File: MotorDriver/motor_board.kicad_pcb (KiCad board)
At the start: 2 copper layers, 60 x 71 mm, 67 parts, among them J1 Conn_01x04_Socket, J10 Conn_01x04_Socket, J4 Screw_Terminal_01x02, J5 Screw_Terminal_01x04, J6 Screw_Terminal_01x04, J7 Conn_01x16_Socket, J8 Conn_01x16_Socket, J9 Conn_01x16_Socket, Q1 AON6411, U1 PCA9685PW, U2 TB6612FNG, U3 TB6612FNG

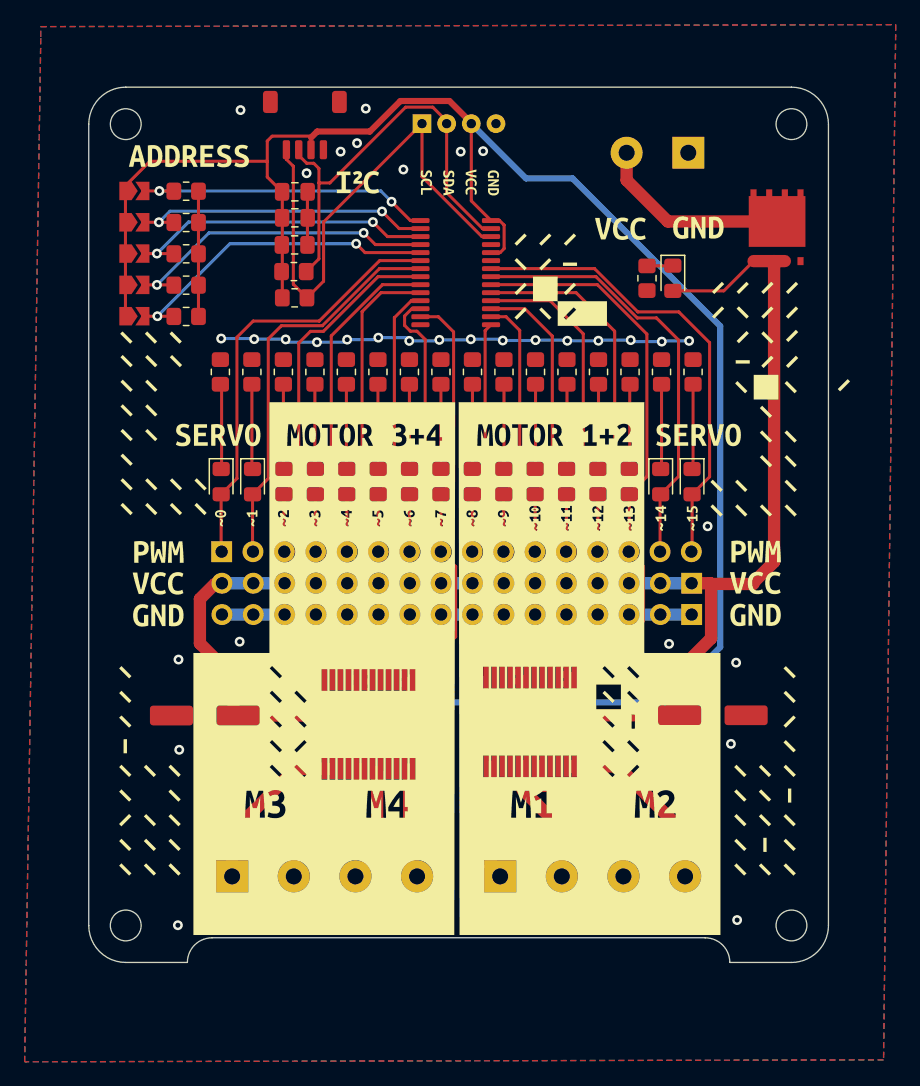
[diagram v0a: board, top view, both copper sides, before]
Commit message: added IMU
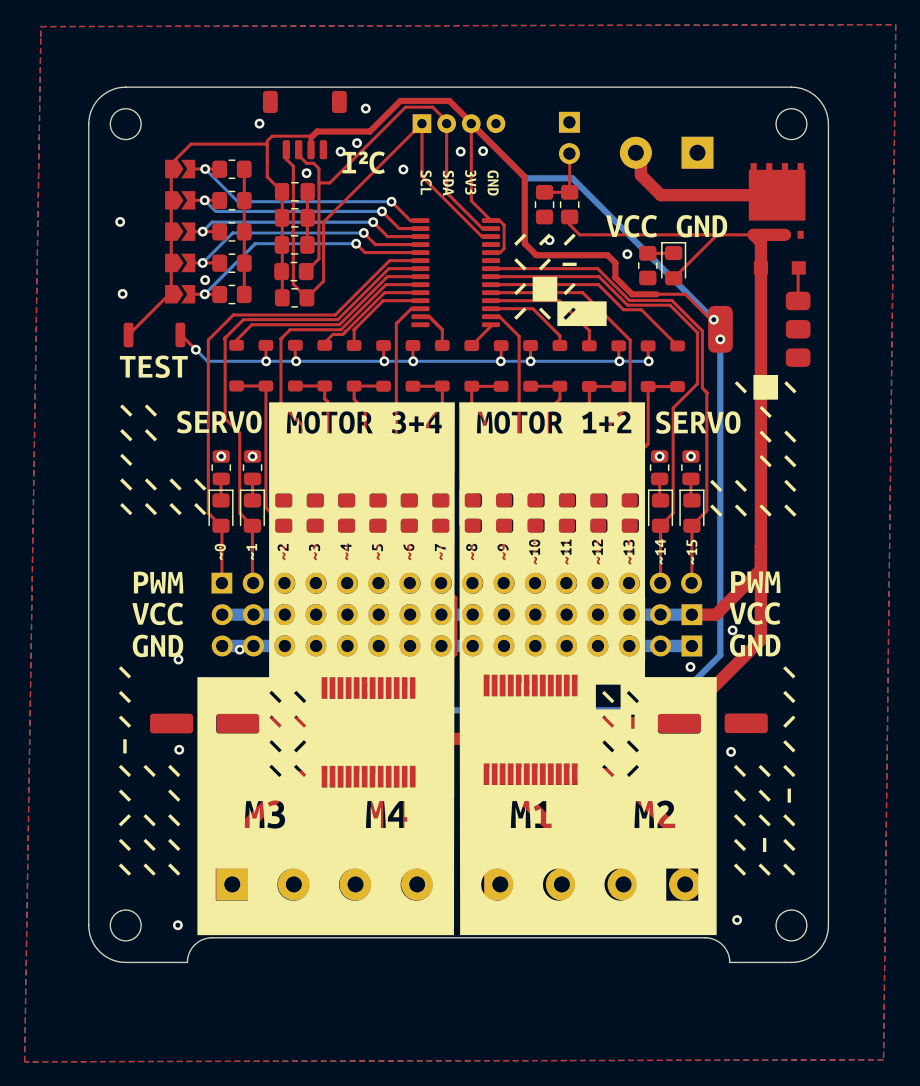
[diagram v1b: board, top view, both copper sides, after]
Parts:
- removed R25: 280, Resistor_SMD:R_0805_2012Metric_Pad1.20x1.40mm_HandSolder
- added CR1: MBR120VLSFT1G, MBR120:SDO_SOD-123FL_ONS, F.Cu at (156.1, 66.7)
- added D1: 1N4148W, Diode_SMD:D_SOD-123, F.Cu at (112.0, 74.6)
- added D19: 1N4148W, Diode_SMD:D_SOD-123, F.Cu at (114.4, 74.6)
- added D20: 1N4148W, Diode_SMD:D_SOD-123, F.Cu at (116.8, 74.6)
- added D21: 1N4148W, Diode_SMD:D_SOD-123, F.Cu at (119.1, 74.6)
- added D22: 1N4148W, Diode_SMD:D_SOD-123, F.Cu at (121.5, 74.6)
- added D23: 1N4148W, Diode_SMD:D_SOD-123, F.Cu at (123.9, 74.6)
- added D24: 1N4148W, Diode_SMD:D_SOD-123, F.Cu at (128.7, 74.6)
- added D25: 1N4148W, Diode_SMD:D_SOD-123, F.Cu at (126.3, 74.6)
- added D26: 1N4148W, Diode_SMD:D_SOD-123, F.Cu at (131.1, 74.6)
- added D27: 1N4148W, Diode_SMD:D_SOD-123, F.Cu at (133.5, 74.6)
- added D28: 1N4148W, Diode_SMD:D_SOD-123, F.Cu at (138.2, 74.6)
- added D29: 1N4148W, Diode_SMD:D_SOD-123, F.Cu at (135.8, 74.6)
- added D30: 1N4148W, Diode_SMD:D_SOD-123, F.Cu at (140.6, 74.6)
- added D31: 1N4148W, Diode_SMD:D_SOD-123, F.Cu at (143.0, 74.6)
- added D32: 1N4148W, Diode_SMD:D_SOD-123, F.Cu at (147.8, 74.6)
- added D33: 1N4148W, Diode_SMD:D_SOD-123, F.Cu at (145.4, 74.6)
- added J3: Conn_01x02_Socket, Connector_PinHeader_2.54mm:PinHeader_1x02_P2.54mm_Vertical, F.Cu at (139.0, 54.9)
- added R26: 1k1, Resistor_SMD:R_0805_2012Metric_Pad1.20x1.40mm_HandSolder, F.Cu at (137.0, 61.5)
- added R27: 3k9, Resistor_SMD:R_0805_2012Metric_Pad1.20x1.40mm_HandSolder, F.Cu at (139.0, 61.5)
- added R8: 270, Resistor_SMD:R_0805_2012Metric, F.Cu at (143.8, 82.9)
- added SW9: SW_Push, Button_Switch_SMD:SW_Push_SPST_NO_Alps_SKRK, F.Cu at (105.3, 72.1)
- added U4: AMS1117, Package_TO_SOT_SMD:SOT-223-3_TabPin2, F.Cu at (154.4, 71.6)
- R10, R11, R12, R13, R14, R15, R16, R17, R18, R19, R20, R21, R22, R23, R24: value 280 -> 270; footprint Resistor_SMD:R_0805_2012Metric_Pad1.20x1.40mm_HandSolder -> Resistor_SMD:R_0805_2012Metric
- moved R23 39.0 mm to (148.8, 82.9)
- moved R24 8.22 mm to (146.3, 82.9)
- moved R10 8.21 mm to (141.2, 82.9)
- moved R11 8.21 mm to (138.7, 82.9)
- moved R12 8.20 mm to (136.1, 82.9)
- moved R13 8.20 mm to (133.6, 82.9)
- moved R14 8.19 mm to (131.1, 82.9)
- moved R15 8.19 mm to (128.5, 82.9)
- moved R16 8.18 mm to (126.0, 82.9)
- moved R17 8.18 mm to (123.4, 82.9)
- moved R18 8.17 mm to (120.9, 82.9)
- moved R19 8.17 mm to (118.4, 82.9)
- moved R20 8.16 mm to (115.8, 82.9)
- moved R21 8.16 mm to (113.3, 82.9)
- moved R22 8.15 mm to (110.7, 82.9)
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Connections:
- D11 pad 2: PWM5 -> PWM5motor
- D12 pad 2: PWM4 -> PWM4motor
- D14 pad 2: PWM2 -> PWM2motor
- D3 pad 2: PWM13 -> PWM13motor
- D5 pad 2: PWM11 -> PWM11motor
- D6 pad 2: PWM10 -> PWM10motor
- D8 pad 2: PWM8 -> PWM8motor
- D9 pad 2: PWM7 -> PWM7motor
- J7 pad 11: PWM10 -> PWM10motor
- J7 pad 12: PWM11 -> PWM11motor
- J7 pad 14: PWM13 -> PWM13motor
- J7 pad 3: PWM2 -> PWM2motor
- J7 pad 5: PWM4 -> PWM4motor
- J7 pad 6: PWM5 -> PWM5motor
- J7 pad 8: PWM7 -> PWM7motor
- J7 pad 9: PWM8 -> PWM8motor
- R10 pad 1: Net-(D3-K) -> Net-(D4-K)
- R11 pad 1: Net-(D4-K) -> Net-(D5-K)
- R12 pad 1: Net-(D5-K) -> Net-(D6-K)
- R13 pad 1: Net-(D6-K) -> Net-(D7-K)
- R14 pad 1: Net-(D7-K) -> Net-(D8-K)
- R15 pad 1: Net-(D8-K) -> Net-(D9-K)
- R16 pad 1: Net-(D9-K) -> Net-(D10-K)
- R17 pad 1: Net-(D10-K) -> Net-(D11-K)
- R18 pad 1: Net-(D11-K) -> Net-(D12-K)
- R19 pad 1: Net-(D12-K) -> Net-(D13-K)
- R20 pad 1: Net-(D13-K) -> Net-(D14-K)
- R21 pad 1: Net-(D14-K) -> Net-(D15-K)
- R22 pad 1: Net-(D15-K) -> Net-(D16-K)
- R23 pad 1: Net-(D16-K) -> Net-(D17-K)
- R24 pad 1: Net-(D17-K) -> Net-(D18-K)
- U2 pad 15: PWM7 -> PWM7motor
- U2 pad 17: PWM5 -> PWM5motor
- U2 pad 21: PWM4 -> PWM4motor
- U2 pad 23: PWM2 -> PWM2motor
- U3 pad 15: PWM13 -> PWM13motor
- U3 pad 17: PWM11 -> PWM11motor
- U3 pad 21: PWM10 -> PWM10motor
- U3 pad 23: PWM8 -> PWM8motor
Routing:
- net testvoltage: track 0.00 -> 48.8 mm, vias 0 -> 9
- net GND: track 91.1 -> 52.6 mm, vias 36 -> 38
- net PWM13motor: track 0.00 -> 34.5 mm
- net VCC: track 158.0 -> 190.6 mm, vias 2 -> 4
- net PWM7motor: track 0.00 -> 32.3 mm
- net PWM10motor: track 0.00 -> 31.2 mm
- net PWM13: track 48.2 -> 17.2 mm
- net PWM11motor: track 0.00 -> 30.3 mm
- net PWM7: track 35.7 -> 5.61 mm
- net PWM2motor: track 0.00 -> 29.7 mm
- net PWM10: track 36.0 -> 7.29 mm
- net PWM4motor: track 0.00 -> 28.7 mm
- net PWM5motor: track 0.00 -> 28.7 mm
- net PWM11: track 38.9 -> 10.2 mm
- net PWM8motor: track 0.00 -> 28.3 mm
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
